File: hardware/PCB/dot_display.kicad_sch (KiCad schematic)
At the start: 33 parts, among them U10 MAX7219, U27 MAX7219, U29 MAX7219, U3 MAX7219, U31 MAX7219, U4 MAX7219, U6 MAX7219, U7 MAX7219

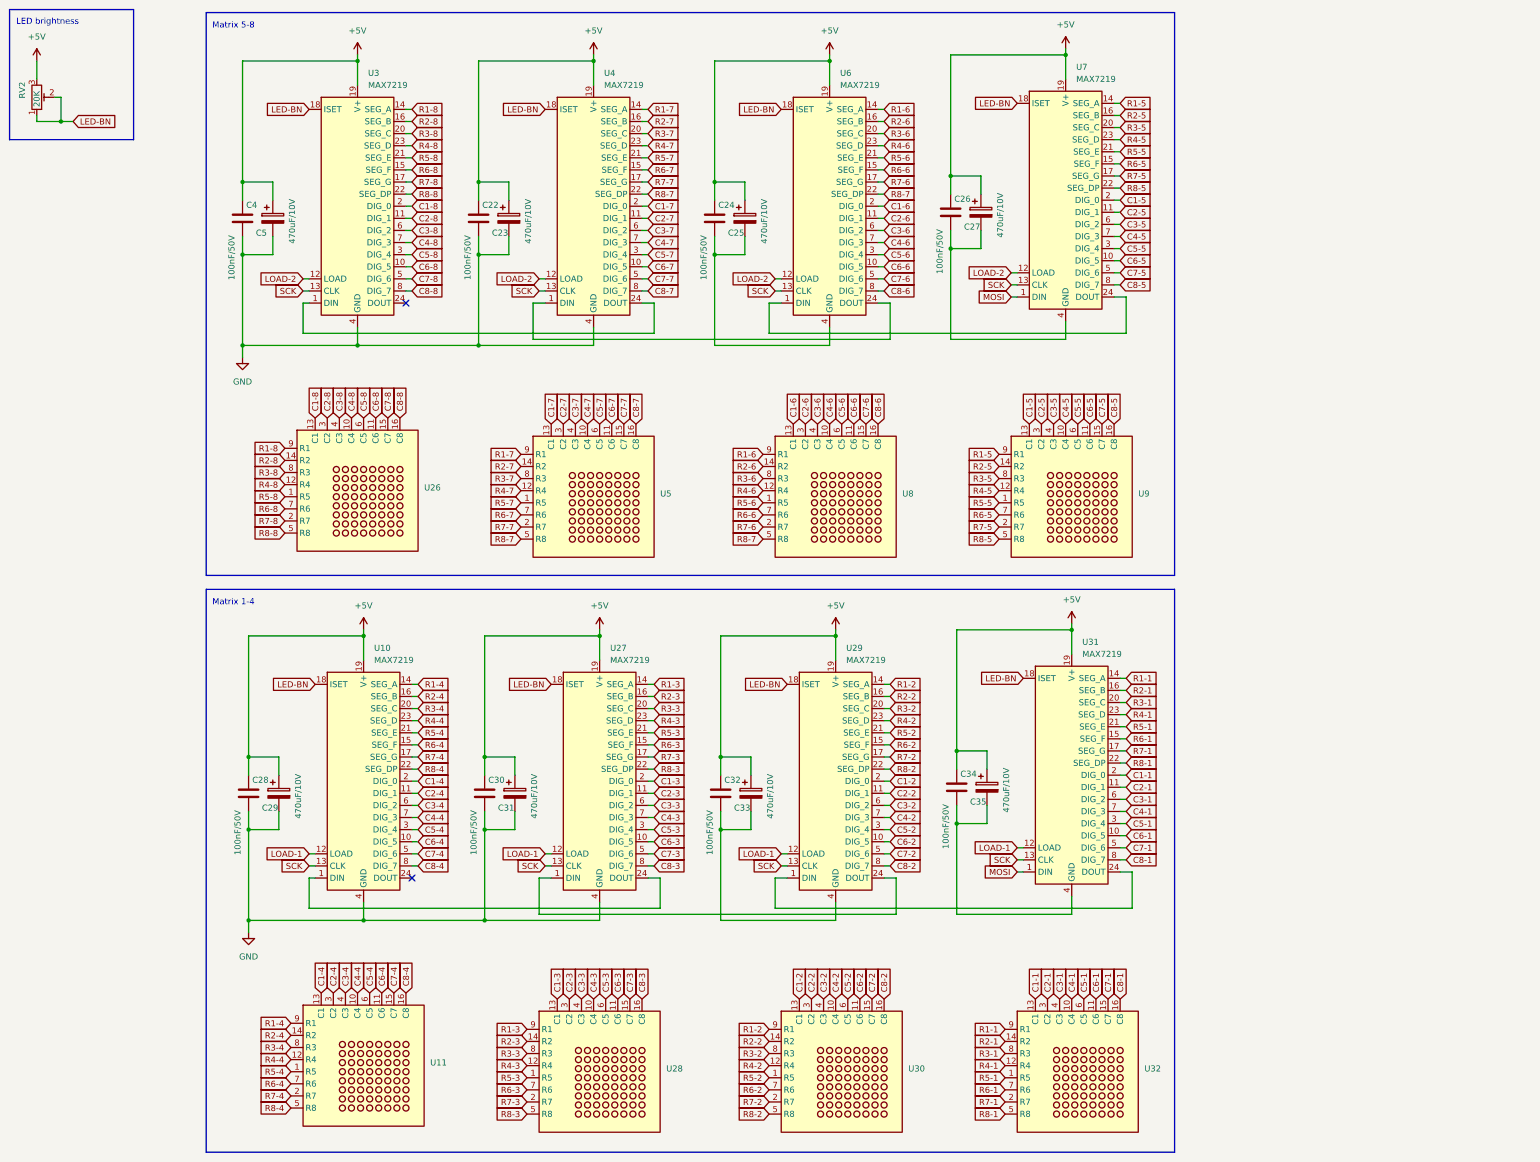
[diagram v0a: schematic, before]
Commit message: KiCAD library MAX7219 added LED driver library updated to access multiple controllers
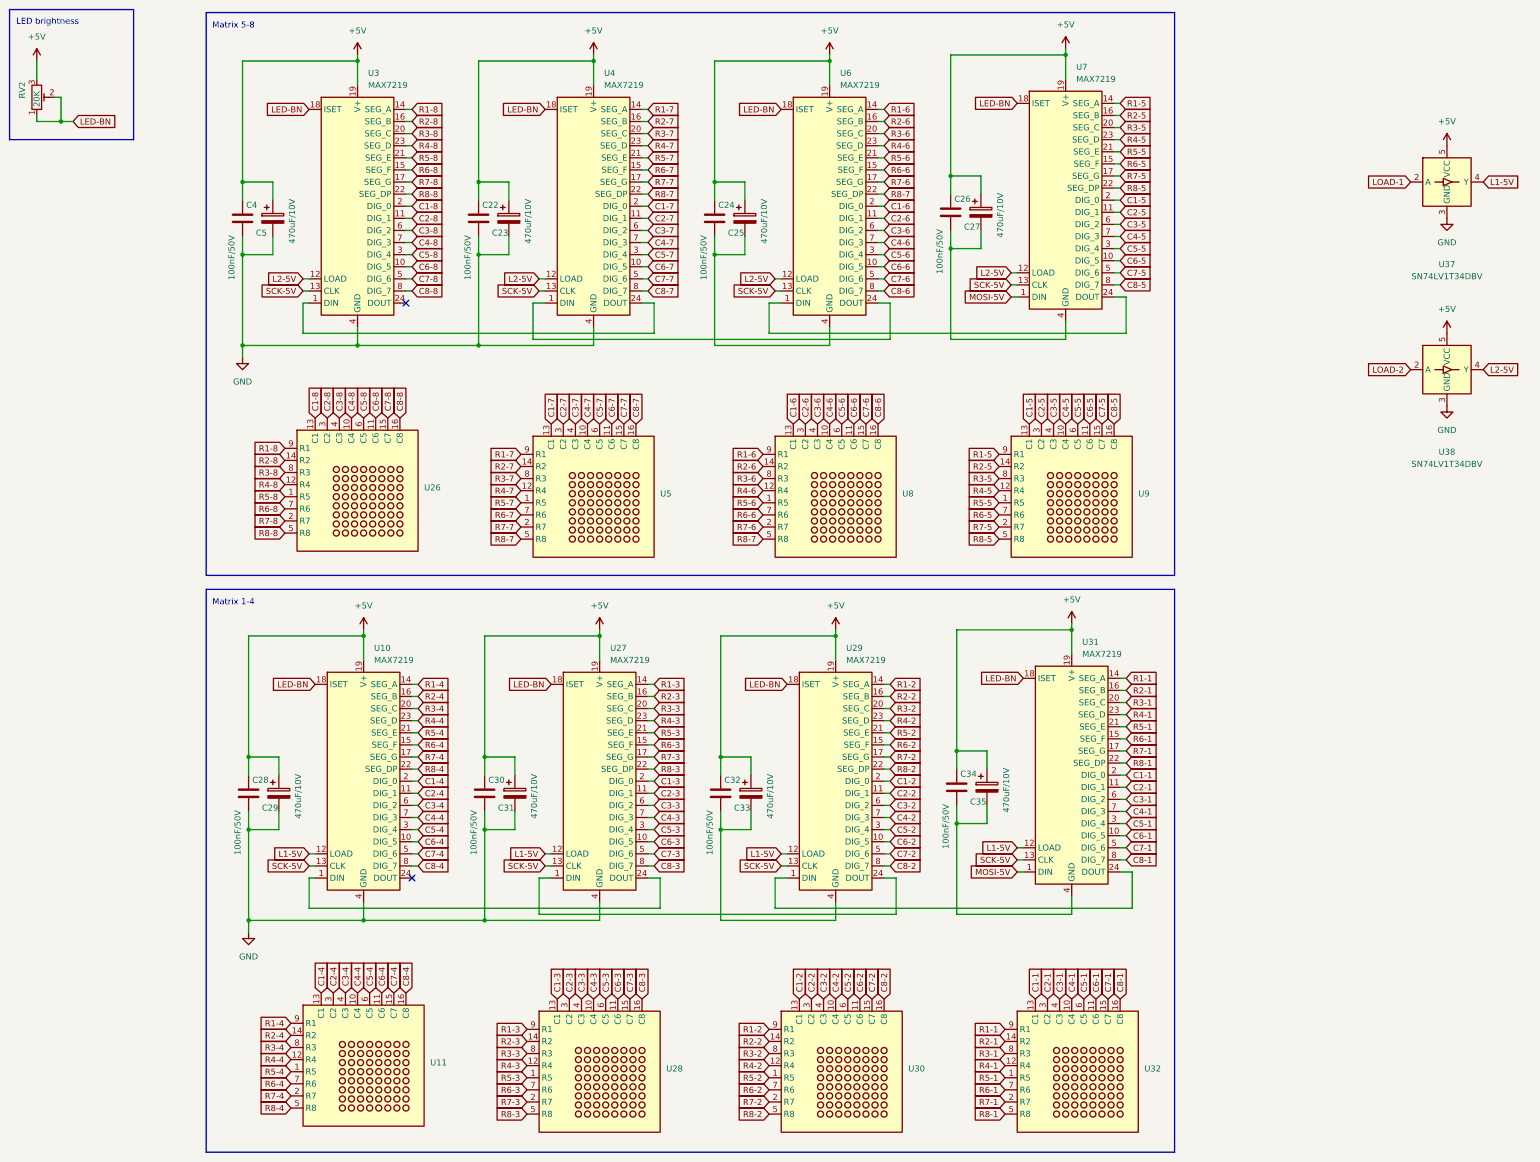
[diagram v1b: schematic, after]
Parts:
- added U37, U38: SN74LV1T34DBV, Package_TO_SOT_SMD:SOT-23-5, symbol Logic_LevelTranslator:SN74LV1T34DBV
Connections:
- net +5V: now also U37.5 (VCC), U38.5 (VCC)
- net GND: now also U37.3 (GND), U38.3 (GND)
- net LOAD-1: now also U37.2 (A); no longer U10.12 (LOAD), U27.12 (LOAD), U29.12 (LOAD), U31.12 (LOAD)
- net LOAD-2: now also U38.2 (A); no longer U3.12 (LOAD), U4.12 (LOAD), U6.12 (LOAD), U7.12 (LOAD)
- net MOSI renamed MOSI-5V
- net SCK renamed SCK-5V
- new net L1-5V: U10.12 (LOAD), U27.12 (LOAD), U29.12 (LOAD), U31.12 (LOAD), U37.4 (Y)
- new net L2-5V: U3.12 (LOAD), U38.4 (Y), U4.12 (LOAD), U6.12 (LOAD), U7.12 (LOAD)

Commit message: capacitors added to signal level converters
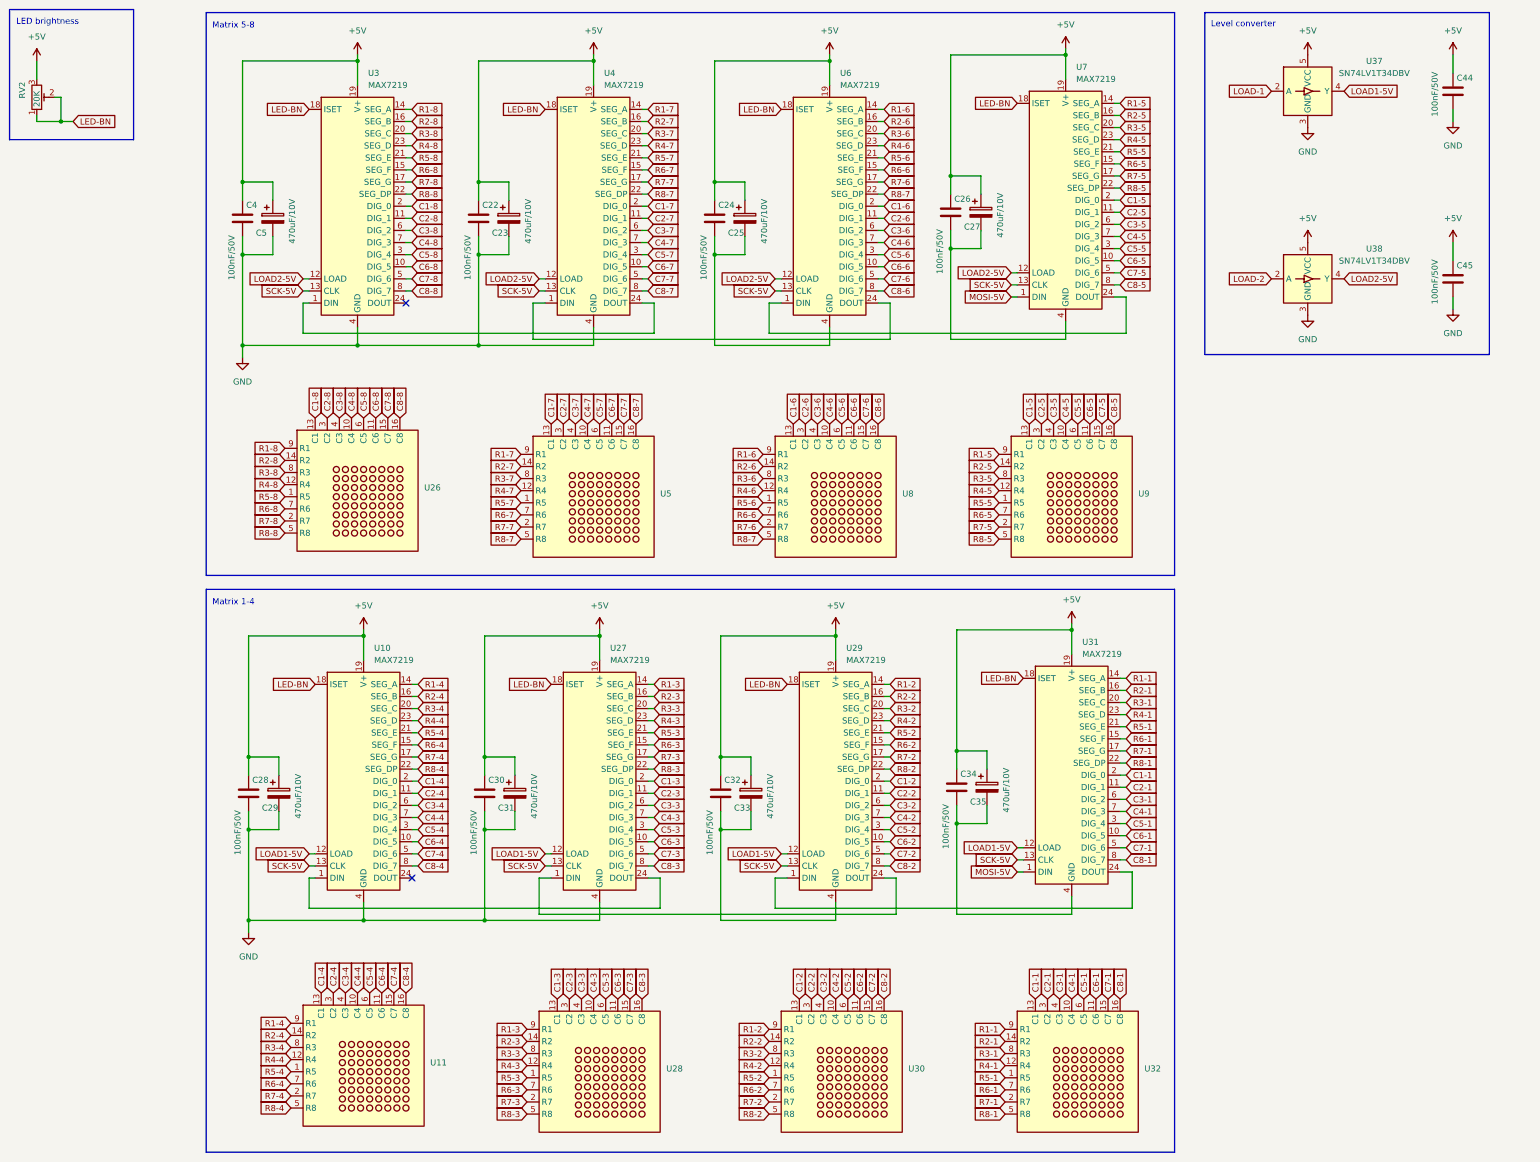
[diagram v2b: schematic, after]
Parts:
- added C44, C45: 100nF/50V, Capacitor_SMD:C_1206_3216Metric_Pad1.33x1.80mm_HandSolder, symbol Device:C
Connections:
- net +5V: now also C44.1, C45.1
- net GND: now also C44.2, C45.2
- net L1-5V renamed LOAD1-5V
- net L2-5V renamed LOAD2-5V
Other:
- note added: "Level converter"

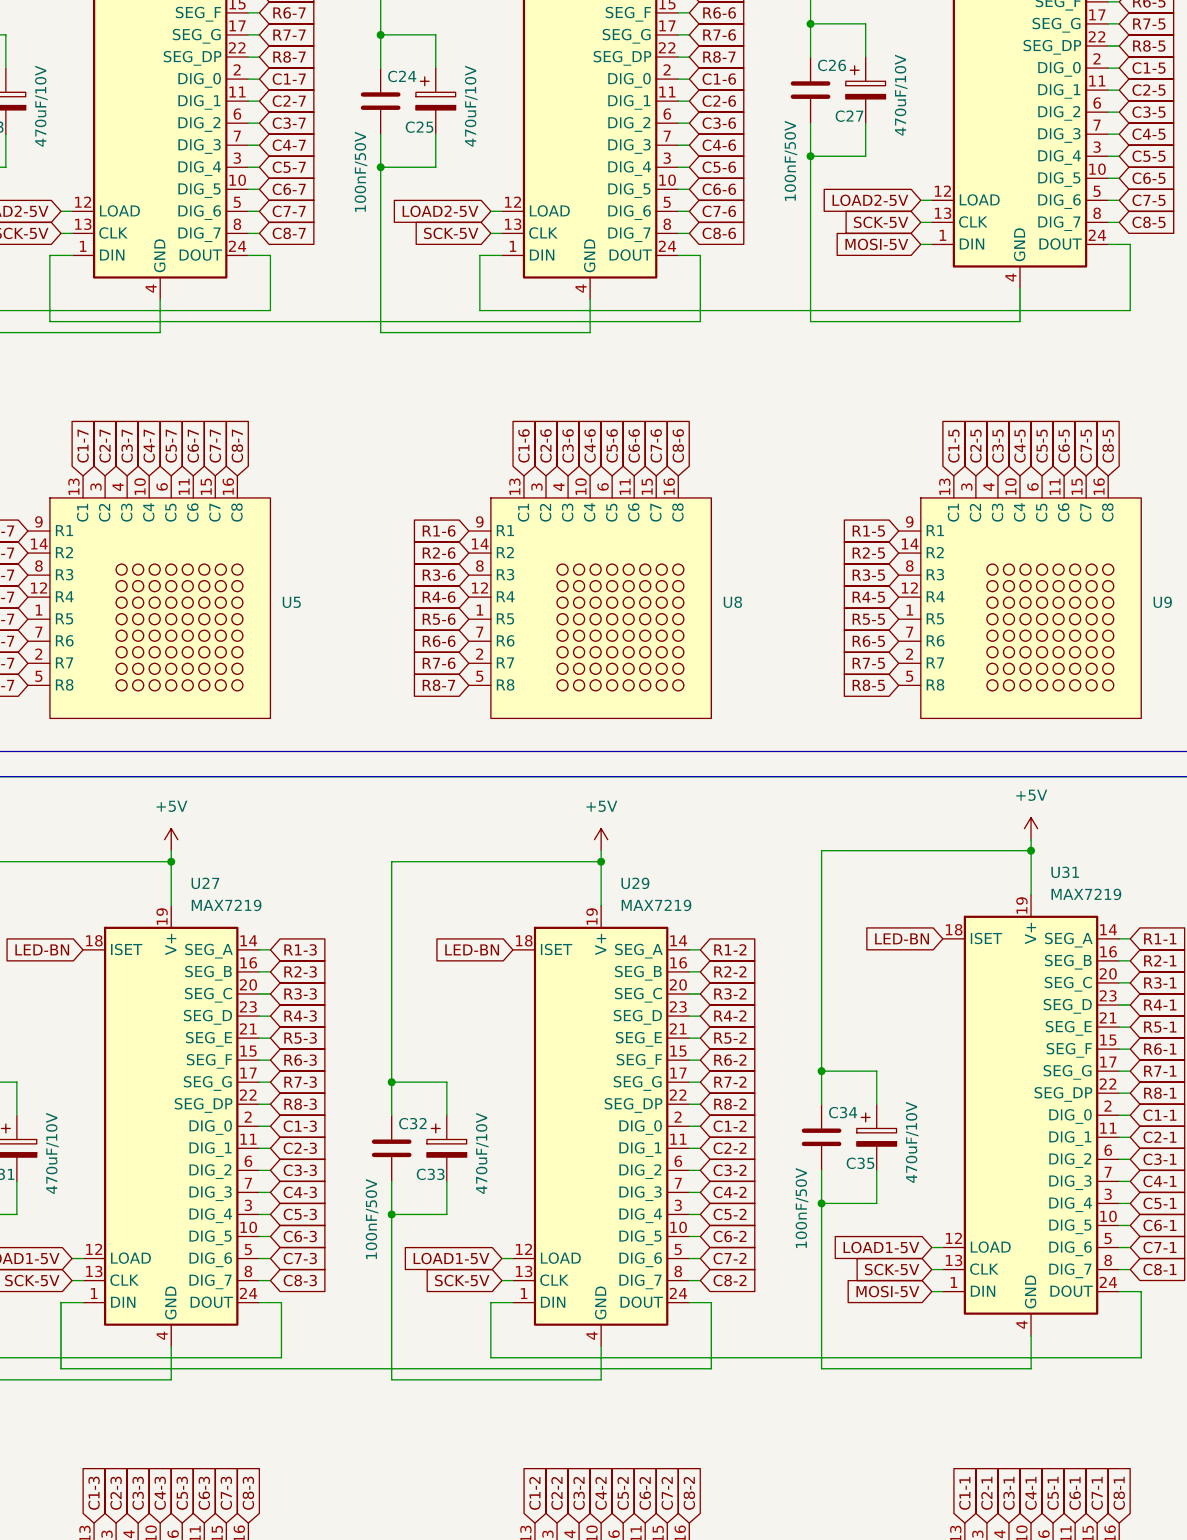
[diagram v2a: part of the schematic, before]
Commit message: missing GND connection to MAX7219 added
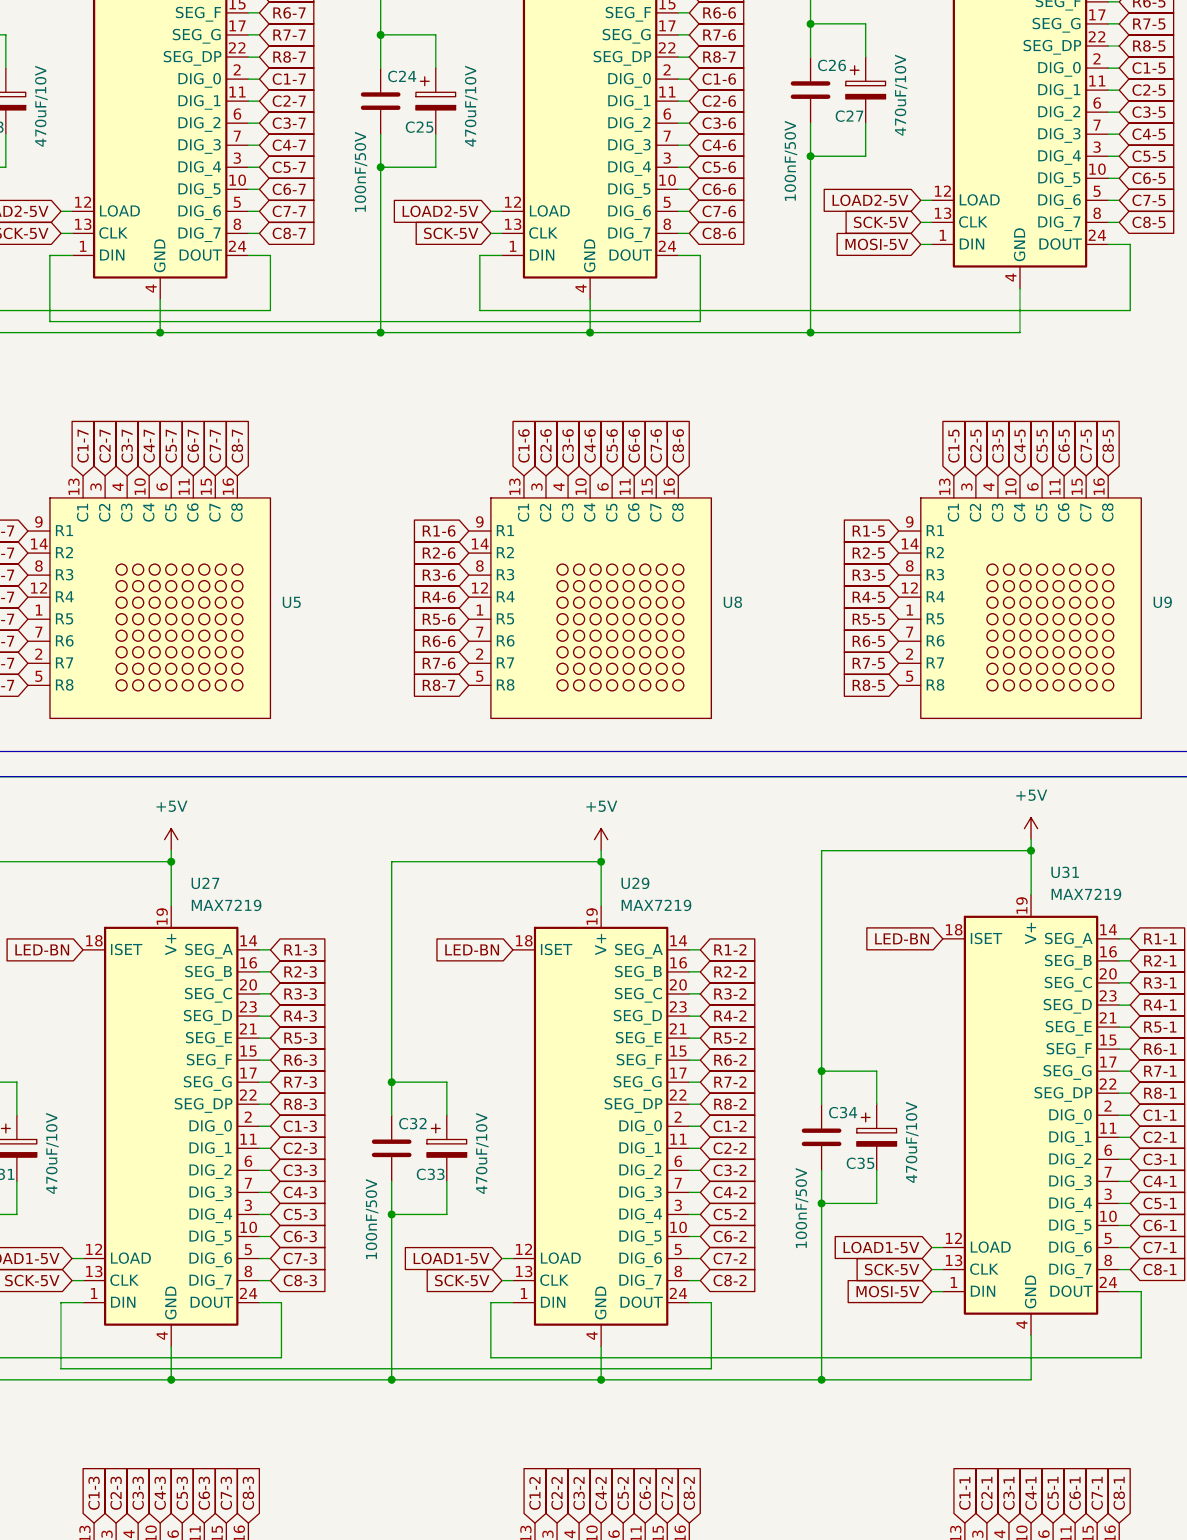
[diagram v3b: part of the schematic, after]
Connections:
- net GND: now also C24.2, C25.2, C26.2, C27.2, C32.2, C33.2, C34.2, C35.2, U29.4 (GND), U29.9 (GND), U31.4 (GND), U31.9 (GND), U6.4 (GND), U6.9 (GND), U7.4 (GND), U7.9 (GND)
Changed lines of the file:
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@@
+	)
+	(junction
+		(at 207.01 215.9)
+		(diameter 0)
+		(color 0 0 0 0)
 	)
 	(junction
@@
 	)
 	(junction
+		(at 182.88 215.9)
+		(diameter 0)
+		(color 0 0 0 0)
+	)
+	(junction
+		(at 231.14 95.25)
+		(diameter 0)
+		(color 0 0 0 0)
+	)
+	(junction
 		(at 107.95 156.21)
 		(diameter 0)
@@
 	)
 	(junction
+		(at 156.21 95.25)
+		(diameter 0)
+		(color 0 0 0 0)
+	)
+	(junction
 		(at 133.35 181.61)
 		(diameter 0)
@@
 	)
 	(junction
+		(at 157.48 215.9)
+		(diameter 0)
+		(color 0 0 0 0)
+	)
+	(junction
+		(at 205.74 95.25)
+		(diameter 0)
+		(color 0 0 0 0)
+	)
+	(junction
 		(at 132.08 60.96)
 		(diameter 0)
@@
 	(junction
 		(at 44.45 48.26)
+		(diameter 0)
+		(color 0 0 0 0)
+	)
+	(junction
+		(at 181.61 95.25)
+		(diameter 0)
+		(color 0 0 0 0)
+	)
+	(junction
+		(at 232.41 215.9)
 		(diameter 0)
 		(color 0 0 0 0)
@@
 	(wire
 		(pts
-			(xy 231.14 93.98) (xy 231.14 74.93)
+			(xy 231.14 95.25) (xy 231.14 74.93)
 		)
 		(stroke
@@
 	(wire
 		(pts
-			(xy 256.54 214.63) (xy 232.41 214.63)
+			(xy 256.54 215.9) (xy 232.41 215.9)
 		)
 		(stroke
@@
 	(wire
 		(pts
-			(xy 232.41 214.63) (xy 232.41 195.58)
+			(xy 232.41 215.9) (xy 232.41 195.58)
 		)
 		(stroke
@@
 	(wire
 		(pts
+			(xy 156.21 95.25) (xy 181.61 95.25)
+		)
+		(stroke
+			(width 0)
+			(type default)
+		)
+	)
+	(wire
+		(pts
 			(xy 218.44 86.36) (xy 218.44 93.98)
 		)
@@
 	(wire
 		(pts
+			(xy 157.48 215.9) (xy 182.88 215.9)
+		)
+		(stroke
+			(width 0)
+			(type default)
+		)
+	)
+	(wire
+		(pts
 			(xy 266.7 72.39) (xy 265.43 72.39)
 		)
@@
 	(wire
 		(pts
+			(xy 205.74 95.25) (xy 231.14 95.25)
+		)
+		(stroke
+			(width 0)
+			(type default)
+		)
+	)
+	(wire
+		(pts
 			(xy 83.82 215.9) (xy 83.82 196.85)
 		)
@@
 	(wire
 		(pts
-			(xy 255.27 90.17) (xy 255.27 93.98)
+			(xy 255.27 90.17) (xy 255.27 95.25)
 		)
 		(stroke
@@
 	(wire
 		(pts
-			(xy 256.54 210.82) (xy 256.54 214.63)
+			(xy 256.54 210.82) (xy 256.54 215.9)
 		)
 		(stroke
@@
 	(wire
 		(pts
+			(xy 207.01 215.9) (xy 232.41 215.9)
+		)
+		(stroke
+			(width 0)
+			(type default)
+		)
+	)
+	(wire
+		(pts
 			(xy 39.37 35.56) (xy 39.37 39.37)
 		)
@@
 	(wire
 		(pts
-			(xy 255.27 93.98) (xy 231.14 93.98)
-		)
-		(stroke
+			(xy 255.27 95.25) (xy 231.14 95.25)
+		)
+		(stroke
